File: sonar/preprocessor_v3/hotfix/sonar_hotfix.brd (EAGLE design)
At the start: 160 x 100 mm, 1 part

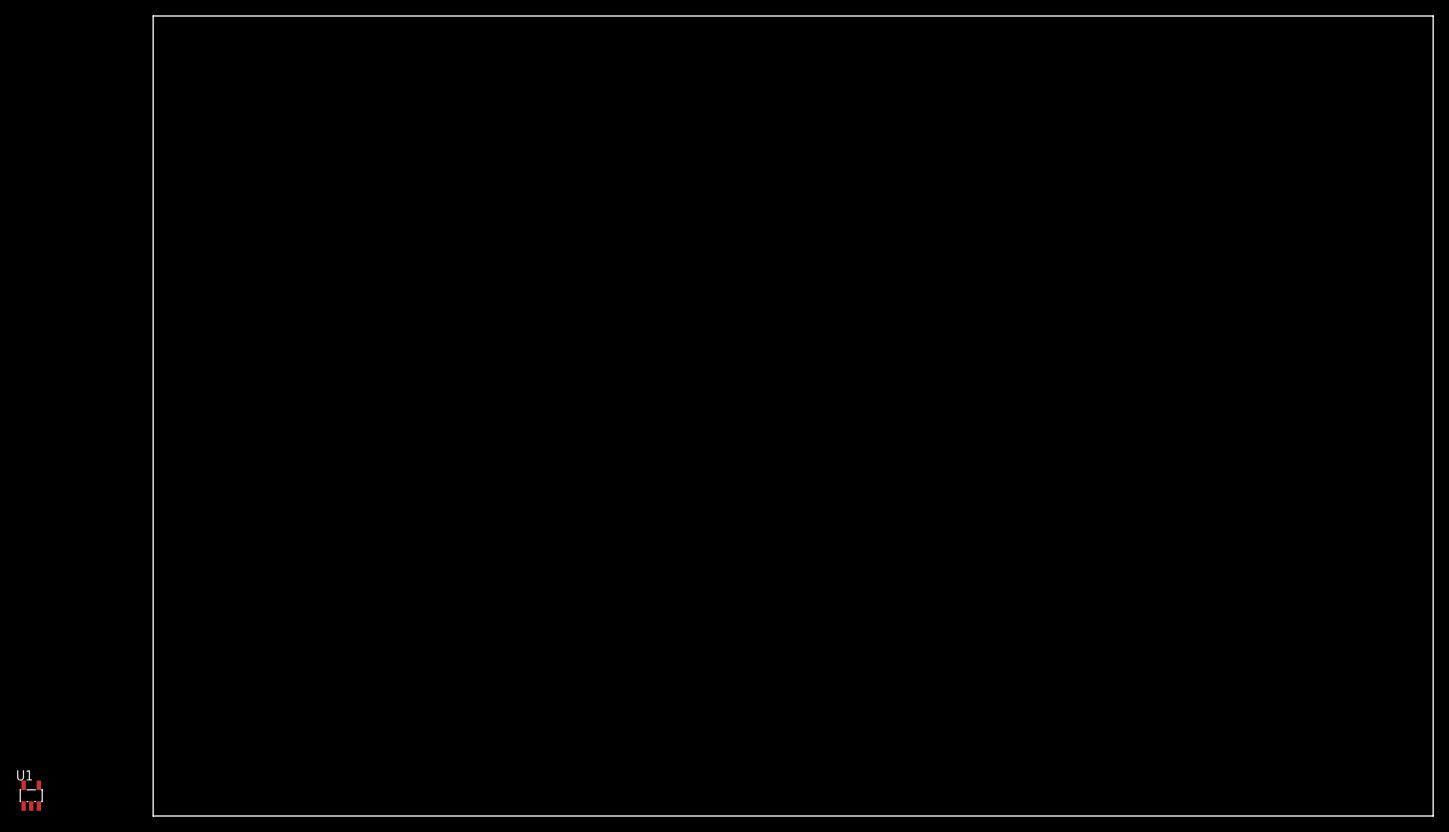
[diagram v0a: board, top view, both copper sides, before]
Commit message: Designed and laid out buffer circuit
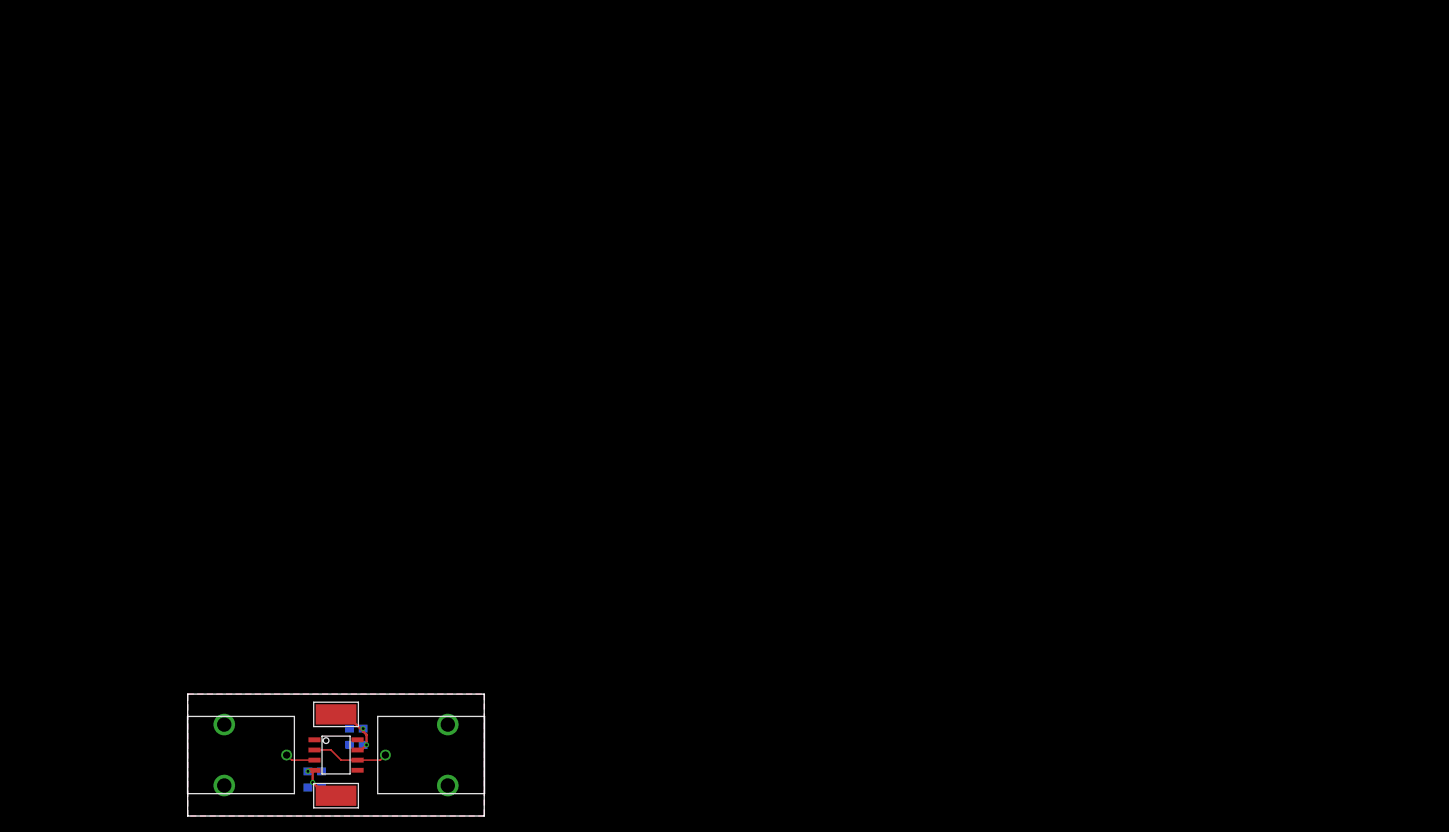
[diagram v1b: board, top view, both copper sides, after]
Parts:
- added C1, C2, C3, C4: (no value), rcl:C0603
- added PAD1, PAD2: WIREPADSMD5-2,5, wirepad:5-2,5
- added X1, X2: (no value), hotfix:0731000105
- U1: device hotfix:SOT23-5 -> hotfix:SO-8
- moved U1 38.4 mm to (22.9, 7.62)
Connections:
- new net +5V: C3.1, C4.1, PAD1.1, U1.7
- new net -5V: C1.1, C2.1, PAD2.1, U1.4
- new net GND: C1.2, C2.2, C3.2, C4.2, X1.P$1, X1.P$2, X2.P$1, X2.P$2
- new net N$1: U1.3, X1.P$3
- new net N$2: U1.2, U1.6, X2.P$3
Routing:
- net N$2: track 0.00 -> 9.65 mm
- net +5V: track 0.00 -> 8.27 mm, vias 0 -> 2
- net -5V: track 0.00 -> 6.98 mm, vias 0 -> 2
- net N$1: track 0.00 -> 3.74 mm
- added copper zone on layer 1, net GND
- added copper zone on layer 16, net GND
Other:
- board size 160 x 100 mm -> 37.1 x 15.2 mm

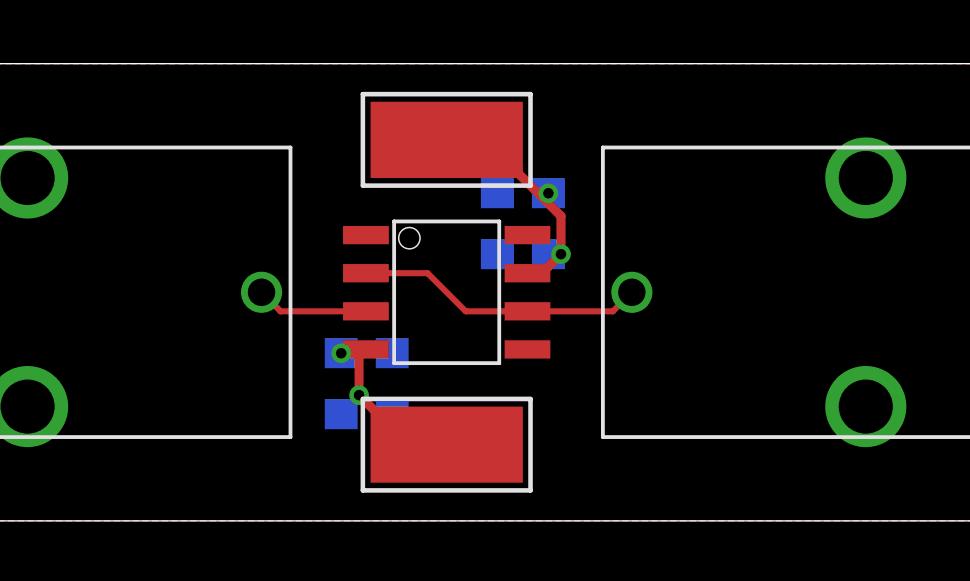
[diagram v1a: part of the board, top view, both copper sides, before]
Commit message: Changed layout of capacitors and wirepads
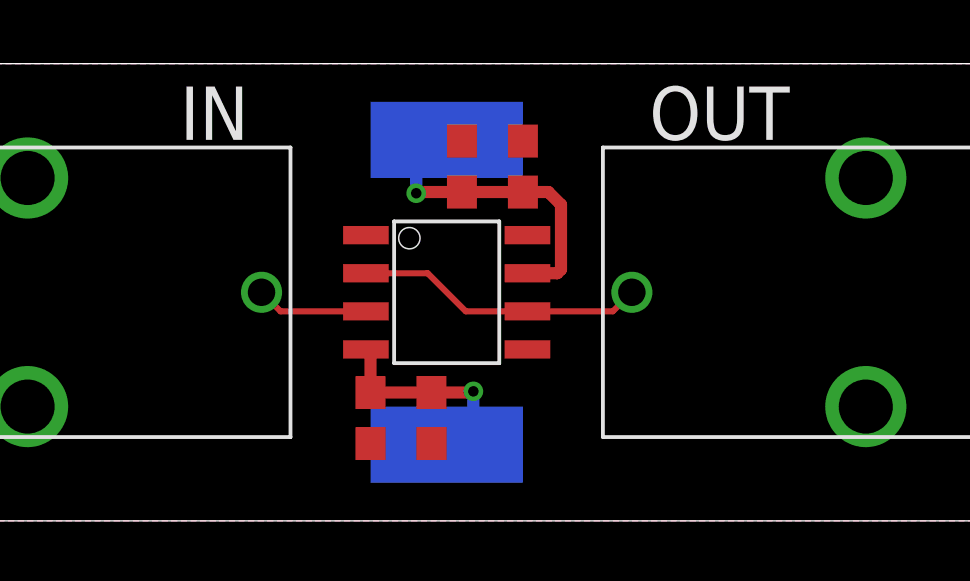
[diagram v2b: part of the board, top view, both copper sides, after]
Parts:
- moved C3 2.92 mm to (25.4, 11.8), flipped to the top, turned to 90 degrees
- moved C4 2.22 mm to (23.4, 11.8), flipped to the top, turned to 90 degrees
- moved C2 2.16 mm to (20.3, 3.43), flipped to the top, turned to 270 degrees
- moved C1 2.16 mm to (22.4, 3.43), flipped to the top, turned to 270 degrees
- flipped PAD1 to the bottom
- flipped PAD2 to the bottom
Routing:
- net +5V: track 8.27 -> 10.5 mm, vias 2 -> 1
- net -5V: track 6.98 -> 7.09 mm, vias 2 -> 1
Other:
- board text added: "IN"
- board text added: "OUT"
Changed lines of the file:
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@@
 <dimension x1="4.318" y1="15.164" x2="4.318" y2="0" x3="1.27" y3="7.582" textsize="1.778" layer="48" unit="inch" visible="yes"/>
 <dimension x1="41.382" y1="15.164" x2="4.318" y2="15.164" x3="22.85" y3="18.034" textsize="1.778" layer="48" unit="inch" visible="yes"/>
+<text x="13.97" y="12.7" size="1.778" layer="21">IN</text>
+<text x="34.29" y="12.7" size="1.778" layer="21" align="bottom-right">OUT</text>
 </plain>
 <attributes>
@@
 <element name="X1" library="hotfix" package="0731000105" value="" x="8.89" y="7.62" rot="R270"/>
 <element name="X2" library="hotfix" package="0731000105" value="" x="36.83" y="7.62" rot="R90"/>
-<element name="PAD1" library="wirepad" library_urn="urn:adsk.eagle:library:412" package="5-2,5" package3d_urn="urn:adsk.eagle:package:30845/1" value="WIREPADSMD5-2,5" x="22.86" y="12.7" smashed="yes" rot="R90">
-<attribute name="VALUE" x="20.06" y="12.6" size="0.0254" layer="27" rot="R90"/>
-</element>
-<element name="PAD2" library="wirepad" library_urn="urn:adsk.eagle:library:412" package="5-2,5" package3d_urn="urn:adsk.eagle:package:30845/1" value="WIREPADSMD5-2,5" x="22.86" y="2.54" smashed="yes" rot="R90">
-<attribute name="VALUE" x="20.06" y="2.44" size="0.0254" layer="27" rot="R90"/>
-</element>
-<element name="C1" library="rcl" library_urn="urn:adsk.eagle:library:334" package="C0603" package3d_urn="urn:adsk.eagle:package:23616/2" value="" x="20.193" y="3.556" smashed="yes" rot="MR180">
-<attribute name="SPICEPREFIX" value="C" x="20.193" y="3.556" size="1.778" layer="28" rot="MR180" display="off"/>
-<attribute name="VALUE" x="19.558" y="5.461" size="1.27" layer="28" rot="MR180"/>
-</element>
-<element name="C2" library="rcl" library_urn="urn:adsk.eagle:library:334" package="C0603" package3d_urn="urn:adsk.eagle:package:23616/2" value="" x="20.193" y="5.588" smashed="yes" rot="MR180">
-<attribute name="SPICEPREFIX" value="C" x="20.193" y="5.588" size="1.778" layer="28" rot="MR180" display="off"/>
-<attribute name="VALUE" x="19.558" y="7.493" size="1.27" layer="28" rot="MR180"/>
-</element>
-<element name="C3" library="rcl" library_urn="urn:adsk.eagle:library:334" package="C0603" package3d_urn="urn:adsk.eagle:package:23616/2" value="" x="25.4" y="8.89" smashed="yes" rot="MR0">
-<attribute name="SPICEPREFIX" value="C" x="25.4" y="8.89" size="1.778" layer="28" rot="MR0" display="off"/>
-<attribute name="VALUE" x="26.035" y="6.985" size="1.27" layer="28" rot="MR0"/>
-</element>
-<element name="C4" library="rcl" library_urn="urn:adsk.eagle:library:334" package="C0603" package3d_urn="urn:adsk.eagle:package:23616/2" value="" x="25.4" y="10.922" smashed="yes" rot="MR0">
-<attribute name="SPICEPREFIX" value="C" x="25.4" y="10.922" size="1.778" layer="28" rot="MR0" display="off"/>
-<attribute name="VALUE" x="26.035" y="9.017" size="1.27" layer="28" rot="MR0"/>
+<element name="PAD1" library="wirepad" library_urn="urn:adsk.eagle:library:412" package="5-2,5" package3d_urn="urn:adsk.eagle:package:30845/1" value="WIREPADSMD5-2,5" x="22.86" y="12.7" smashed="yes" rot="MR90"/>
+<element name="PAD2" library="wirepad" library_urn="urn:adsk.eagle:library:412" package="5-2,5" package3d_urn="urn:adsk.eagle:package:30845/1" value="WIREPADSMD5-2,5" x="22.86" y="2.54" smashed="yes" rot="MR90"/>
+<element name="C1" library="rcl" library_urn="urn:adsk.eagle:library:334" package="C0603" package3d_urn="urn:adsk.eagle:package:23616/2" value="" x="22.352" y="3.429" smashed="yes" rot="R270">
+<attribute name="SPICEPREFIX" value="C" x="22.352" y="3.429" size="1.778" layer="27" rot="R270" display="off"/>
+<attribute name="VALUE" x="20.447" y="4.064" size="1.27" layer="27" rot="R270"/>
+</element>
+<element name="C2" library="rcl" library_urn="urn:adsk.eagle:library:334" package="C0603" package3d_urn="urn:adsk.eagle:package:23616/2" value="" x="20.32" y="3.429" smashed="yes" rot="R270">
+<attribute name="SPICEPREFIX" value="C" x="20.32" y="3.429" size="1.778" layer="27" rot="R270" display="off"/>
+<attribute name="VALUE" x="18.415" y="4.064" size="1.27" layer="27" rot="R270"/>
+</element>
+<element name="C3" library="rcl" library_urn="urn:adsk.eagle:library:334" package="C0603" package3d_urn="urn:adsk.eagle:package:23616/2" value="" x="25.4" y="11.811" smashed="yes" rot="R90">
+<attribute name="SPICEPREFIX" value="C" x="25.4" y="11.811" size="1.778" layer="27" rot="R90" display="off"/>
+<attribute name="VALUE" x="27.305" y="11.176" size="1.27" layer="27" rot="R90"/>
+</element>
+<element name="C4" library="rcl" library_urn="urn:adsk.eagle:library:334" package="C0603" package3d_urn="urn:adsk.eagle:package:23616/2" value="" x="23.368" y="11.811" smashed="yes" rot="R90">
+<attribute name="SPICEPREFIX" value="C" x="23.368" y="11.811" size="1.778" layer="27" rot="R90" display="off"/>
+<attribute name="VALUE" x="25.273" y="11.176" size="1.27" layer="27" rot="R90"/>
 </element>
 </elements>
@@
 <contactref element="C3" pad="1"/>
 <contactref element="C4" pad="1"/>
-<wire x1="22.86" y1="12.7" x2="24.13" y2="12.7" width="0.3048" layer="1"/>
-<wire x1="24.13" y1="12.7" x2="26.25" y2="10.58" width="0.3048" layer="1"/>
-<wire x1="26.67" y1="10.16" x2="26.67" y2="8.89" width="0.3048" layer="1"/>
-<wire x1="26.67" y1="8.89" x2="26.035" y2="8.255" width="0.3048" layer="1"/>
-<wire x1="26.035" y1="8.255" x2="25.5524" y2="8.255" width="0.3048" layer="1"/>
-<wire x1="26.67" y1="10.16" x2="26.25" y2="10.58" width="0.3048" layer="1"/>
-<wire x1="26.25" y1="10.58" x2="26.25" y2="10.922" width="0.3048" layer="1"/>
-<via x="26.25" y="10.922" extent="1-16" drill="0.35"/>
-<wire x1="26.25" y1="8.89" x2="26.67" y2="8.89" width="0.3048" layer="16"/>
-<via x="26.67" y="8.89" extent="1-16" drill="0.35"/>
+<wire x1="23.368" y1="10.961" x2="25.4" y2="10.961" width="0.4064" layer="1"/>
+<wire x1="25.4" y1="10.961" x2="26.25" y2="10.961" width="0.4064" layer="1"/>
+<wire x1="26.25" y1="10.961" x2="26.67" y2="10.541" width="0.4064" layer="1"/>
+<wire x1="26.67" y1="8.382" x2="26.543" y2="8.255" width="0.4064" layer="1"/>
+<wire x1="26.543" y1="8.255" x2="25.5524" y2="8.255" width="0.4064" layer="1"/>
+<wire x1="26.67" y1="10.541" x2="26.67" y2="8.382" width="0.4064" layer="1"/>
+<wire x1="23.368" y1="10.961" x2="21.883" y2="10.961" width="0.4064" layer="1"/>
+<wire x1="21.883" y1="10.961" x2="21.844" y2="10.922" width="0.4064" layer="1"/>
+<via x="21.844" y="10.922" extent="1-16" drill="0.35"/>
+<wire x1="21.844" y1="10.922" x2="21.844" y2="11.684" width="0.4064" layer="16"/>
+<wire x1="21.844" y1="11.684" x2="22.86" y2="12.7" width="0.4064" layer="16"/>
 </signal>
 <signal name="-5V">
@@
 <contactref element="C2" pad="1"/>
 <contactref element="C1" pad="1"/>
-<wire x1="22.86" y1="2.54" x2="21.59" y2="2.54" width="0.3048" layer="1"/>
-<wire x1="19.939" y1="4.191" x2="19.939" y2="5.4864" width="0.3048" layer="1"/>
-<wire x1="19.939" y1="5.4864" x2="20.1676" y2="5.715" width="0.3048" layer="1"/>
-<via x="19.939" y="4.191" extent="1-16" drill="0.35"/>
-<wire x1="21.59" y1="2.54" x2="19.939" y2="4.191" width="0.3048" layer="1"/>
-<wire x1="19.939" y1="4.191" x2="19.939" y2="4.152" width="0.3048" layer="16"/>
-<wire x1="19.939" y1="4.152" x2="19.343" y2="3.556" width="0.3048" layer="16"/>
-<wire x1="20.1676" y1="5.715" x2="20.0406" y2="5.588" width="0.3048" layer="1"/>
-<wire x1="20.0406" y1="5.588" x2="19.343" y2="5.588" width="0.3048" layer="1"/>
-<via x="19.343" y="5.588" extent="1-16" drill="0.35"/>
+<wire x1="22.352" y1="4.279" x2="20.32" y2="4.279" width="0.4064" layer="1"/>
+<wire x1="20.32" y1="4.279" x2="20.32" y2="5.5626" width="0.4064" layer="1"/>
+<wire x1="20.32" y1="5.5626" x2="20.1676" y2="5.715" width="0.4064" layer="1"/>
+<wire x1="22.352" y1="4.279" x2="23.71" y2="4.279" width="0.4064" layer="1"/>
+<wire x1="23.71" y1="4.279" x2="23.749" y2="4.318" width="0.4064" layer="1"/>
+<via x="23.749" y="4.318" extent="1-16" drill="0.35"/>
+<wire x1="23.749" y1="4.318" x2="23.749" y2="3.429" width="0.4064" layer="16"/>
+<wire x1="23.749" y1="3.429" x2="22.86" y2="2.54" width="0.4064" layer="16"/>
 </signal>
 <signal name="GND">
